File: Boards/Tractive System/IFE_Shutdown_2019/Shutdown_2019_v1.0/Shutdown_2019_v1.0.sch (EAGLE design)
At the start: 6 parts, among them J1 USB_, U1 FT232RLSSOP

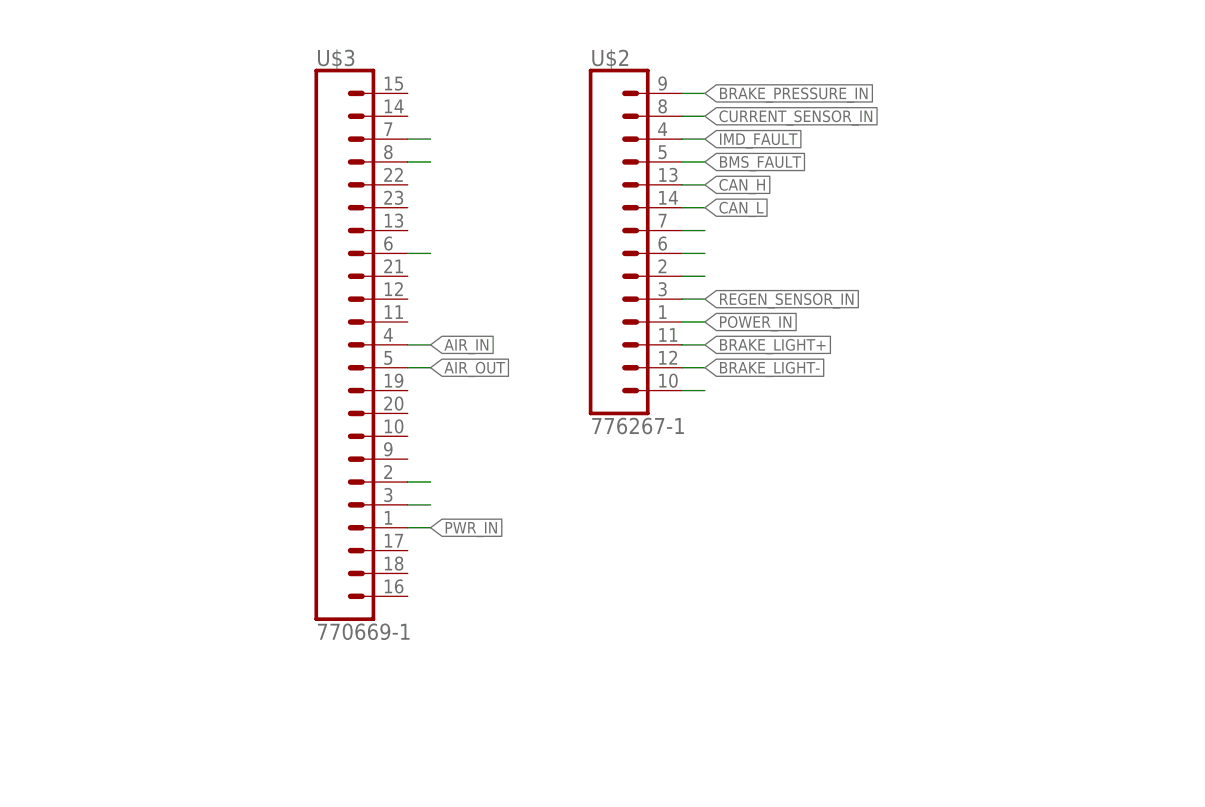
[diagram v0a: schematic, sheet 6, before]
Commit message: Adjusted precharge relay package, reduced area
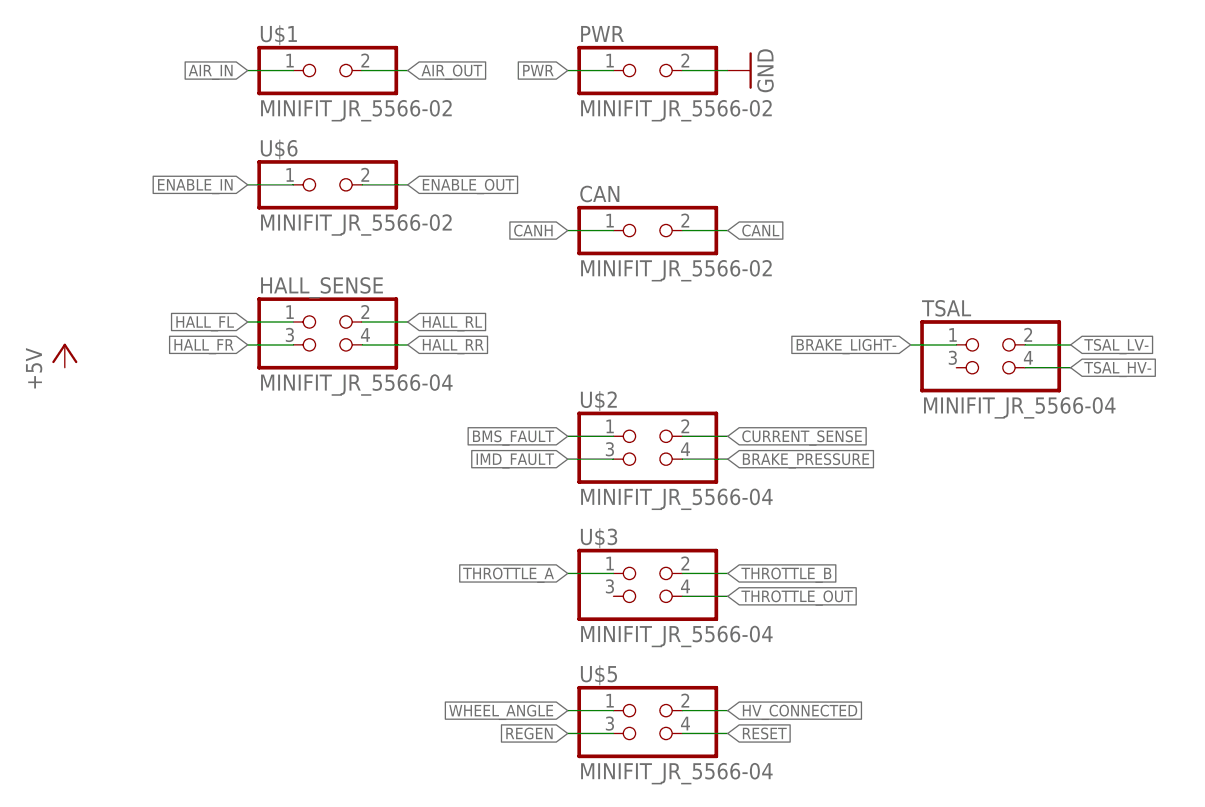
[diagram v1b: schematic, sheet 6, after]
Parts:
- removed J1: USB_, SparkFun-Connectors:USB_
- removed U1: FT232RLSSOP, SparkFun-DigitalIC:FT232RLSSOP
- added !BSPD_FAULT, !CONFLICT, BCO, BTH, TCO, TTH: TPTP09R, testpad:TPTP09R
- added BRAKE, THROTTLE: RTRIM3249W, Resistors:RTRIM3249W
- added C18: 10uF, Capacitors:C0805
- added C19: 0.01uF, Capacitors:C0805
- added C24: 0.1uF, Capacitors:C0805
- added CAN, PWR, U$6: MINIFIT_JR_5566-02, Display_Custom:MINIFIT_JR_5566-02
- added HALL_SENSE, TSAL, U$5: MINIFIT_JR_5566-04, Display_Custom:MINIFIT_JR_5566-04
- added IC1: LM555D, bspd2:LM555D
- added IC3: LM393D, IC's:LM393D
- added Q1, Q2: IRLML6346PBF, TRANS:IRLML6346PBF
- added R10: 1k, Resistors:R0805
- added R13: 50k, Resistors:R0805
- added R14, R33, R38, R39, R40, R8: 10k, Resistors:R0805
- added R9: 100k, Resistors:R0805
- added U$11: SN74LVC1G04DBVR, Display_Custom:SN74LVC1G04DBVR
- added U$7, U$8: IRLL024ZPBF, Display_Custom:IRLL024ZPBF
- added U$9: SN74LVC1G132DBVR, Display_Custom:SN74LVC1G132DBVR
- U$1: value ATTINY84ATTINY84-20MU -> MINIFIT_JR_5566-02; device SparkFun-DigitalIC:ATTINY84ATTINY84-20MU -> Display_Custom:MINIFIT_JR_5566-02
- U$2: value 776267-1 -> MINIFIT_JR_5566-04; device IFE_AMPSEAL_Conn:776267-1 -> Display_Custom:MINIFIT_JR_5566-04
- U$3: value 770669-1 -> MINIFIT_JR_5566-04; device IFE_AMPSEAL_Conn:770669-1 -> Display_Custom:MINIFIT_JR_5566-04
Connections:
- net POWER_IN renamed BRAKE_PRESSURE
- removed net BRAKE_LIGHT+: U$2.3
- removed net BRAKE_PRESSURE_IN: U$2.14
- removed net CAN_H: U$2.10
- removed net CAN_L: U$2.9
- removed net CURRENT_SENSOR_IN: U$2.13
- removed net N$1: U$2.8
- removed net N$2: U$2.7
- removed net N$4: U$2.1
- removed net N$8: U$3.22
- removed net N$9: U$3.17
- removed net PWR_IN: U$3.5
- removed net REGEN_SENSOR_IN: U$2.5
- new net !CONFLICT: !CONFLICT.TP, IC1.TR, R8.2, U$9.Y
- new net +12V: R10.1, R9.1
- new net +5V: BRAKE.A, C24.1, IC1.R, IC1.V+, IC3P.V+, R13.2, R14.2, R33.2, R38.2, R39.2, R40.1, R8.1, THROTTLE.A, U$11.V+, U$9.V+
- new net BRAKE_IN: IC3A.+IN, R33.1
- new net BSPD_FAULT: IC1.Q, U$11.A
- new net CANH: CAN.1
- new net CANL: CAN.2
- new net CURRENT_IN: IC3B.+IN, R14.1
- new net CURRENT_SENSE: U$2.2
- new net ENABLE_IN: U$6.1
- new net ENABLE_OUT: U$6.2
- new net FAULT_1_BSPD_IN: Q2.D, R10.2
- new net GND: BRAKE.E, C18.2, C19.2, C24.2, IC1.GND, IC3P.V-, PWR.2, Q1.S, Q2.S, THROTTLE.E, U$11.GND, U$9.GND
- new net HALL_FL: HALL_SENSE.1
- new net HALL_FR: HALL_SENSE.3
- new net HALL_RL: HALL_SENSE.2
- new net HALL_RR: HALL_SENSE.4
- new net HV_CONNECTED: U$5.2
- new net N$10: C18.1, IC1.DIS, IC1.THR, R13.1
- new net N$11: C19.1, IC1.CV
- new net N$15: Q1.D, Q2.G, R9.2
- new net N$16: IC3B.-IN, THROTTLE.S, TTH.TP
- new net PWR: PWR.1
- new net REGEN: U$5.3
- new net RESET: U$5.4
- new net THROTTLE_A: U$3.1
- new net THROTTLE_B: U$3.2
- new net THROTTLE_OUT: U$3.4
- new net TSAL_HV-: TSAL.4
- new net TSAL_LV-: TSAL.2
- new net WHEEL_ANGLE: U$5.1
- net AIR_IN: now also U$1.1; no longer U$3.13
- net AIR_OUT: now also U$1.2; no longer U$3.12
- net BMS_FAULT: now also U$2.1; no longer U$2.11
- net BRAKE_LIGHT-: now also TSAL.1; no longer U$2.2
- net IMD_FAULT: now also U$2.3; no longer U$2.12
- net N$3: now also IC3B.OUT, R39.1, TCO.TP, U$9.A; no longer U$2.6
- net N$5: now also BCO.TP, IC3A.OUT, R38.1, U$9.B; no longer U$3.21
- net N$6: now also BRAKE.S, BTH.TP, IC3A.-IN; no longer U$3.6
- net N$7: now also !BSPD_FAULT.TP, Q1.G, R40.2, U$11.Y; no longer U$3.7
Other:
- note added: "5V-12V Conversion"
- note added: "Brake Threshold Comparator"
- note added: "Conflict Timer"
- note added: "Current Threshold Comparator"

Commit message: More shutdown work
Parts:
- added BMS1, BSPD, IMD: 3.3v BLUE, led:LEDCHIPLED_0805
- added C1, C3, C4: 0.1uF, Capacitors:C0805
- added C14, C15, C16: 47uF, rcl:CPOL-USUD-6,3X5,8
- added D15, D2, D9: 1N914, Diodes:1N914
- added D3, D5, D6: SMAJ12A, Diodes:SMAJ12A
- added Q11, Q15, Q6: DMP3099L-7, TRANS:DMP3099L-7
- added Q16, Q3, Q5: DMN6140L-7, TRANS:DMN6140L-7
- added R1, R19, R24: 10k, Resistors:R0805
- added R11, R20, R23: 300, Resistors:R0805
- added R3, R5, R6: 100k, Resistors:R0805
- added R36: 1k, Resistors:R0805
- added U$10, U$12, U$13: PCN-112D3MHZ, Display_Custom:PCN-112D3MHZ
- U$4, U$7, U$8: value IRLL024ZPBF -> RT424012; device Display_Custom:IRLL024ZPBF -> Display_Custom:RT424012
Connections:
- new net BMS1_FAULT_INDICATOR: C15.+, D9.C, R20.1, U$7.2_CENTER, U$7.COIL+
- new net BSPD_FAULT_INDICATOR: C16.+, D2.C, R11.1, U$4.2_CENTER, U$4.COIL+
- new net FAULT_2_BMS: Q3.G, R1.2
- new net FAULT_3_BMS2_IN: C3.1, D5.C, R5.2
- new net FAULT_4_IMD_IN: C4.1, D6.C, Q16.G, R24.2, R6.2
- new net FAULT_RESET: Q11.G, Q15.G, Q6.G, R36.2
- new net IMD_FAULT_INDICATOR: C14.+, D15.C, R23.1, U$8.2_CENTER, U$8.COIL+
- new net N$1: C15.-, D9.A, Q3.D, U$7.COIL-
- new net N$27: U$4.1_ACTIVE, U$7.1_CENTER
- new net N$28: Q6.D, U$4.2_REST
- new net N$31: U$7.1_ACTIVE, U$8.1_CENTER
- new net N$32: C16.-, D2.A, Q5.D, U$4.COIL-
- new net N$34: BMS1.A, R20.2
- new net N$35: Q11.D, U$7.2_REST
- new net N$42: IMD.A, R23.2
- new net N$43: Q15.D, U$8.2_REST
- new net N$44: C14.-, D15.A, Q16.D, U$8.COIL-
- new net N$8: BSPD.A, R11.2
- net +12V: now also Q11.S, Q15.S, Q6.S, R36.1, U$4.2_ACTIVE, U$7.2_ACTIVE, U$8.2_ACTIVE
- net AIR_IN: now also U$4.1_CENTER
- net AIR_OUT: now also U$8.1_ACTIVE
- net FAULT_1_BSPD_IN: now also C1.1, D3.C, Q5.G, R19.2, R3.2
- net GND: now also BMS1.C, BSPD.C, C1.2, C3.2, C4.2, D3.A, D5.A, D6.A, IMD.C, Q16.S, Q3.S, Q5.S, R1.1, R19.1, R24.1, R3.1, R5.1, R6.1
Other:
- note added: "FAULT_RESET Pull Up"
- note added: "Fault Circuitry Faults are Active Low Pull FAULT_RESET Low to Reset"
- note added: "Fault Input Filter"

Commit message: Adding circuitry to shutdown, relay drivers
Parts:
- removed U$12: PCN-112D3MHZ, Display_Custom:PCN-112D3MHZ
- added H1, H2, H3, H4: MOUNT-PAD-ROUND3.0, holes:MOUNT-PAD-ROUND3.0
- added Q4, Q7, Q8: DMN6140L-7, TRANS:DMN6140L-7
- added R2, R4, R7: 10k, Resistors:R0805
- added R_RTD: PCN-112D3MHZ, Display_Custom:PCN-112D3MHZ
- added U1, U2: STM32F103CBT6, ST Microelctronics_By_element14_Batch_1:STM32F103CBT6
- renumbered BMS1 to BMS, U$10 to R_APPS, U$13 to R_BTSF, U$4 to R_BSPD, U$7 to R_BMS, U$8 to R_IMD
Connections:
- new net APPS_EN: Q4.G, R2.2
- new net BTSF_EN: Q7.G, R4.2
- new net N$12: R_BTSF.3, R_RTD.4
- new net N$13: R_APPS.3, R_BTSF.4
- new net N$2: Q4.D, R_APPS.2
- new net N$4: Q7.D, R_BTSF.2
- new net N$9: Q8.D, R_RTD.2
- new net PRECHARGE_COMPLETE: U$3.3
- new net RTDS-: TSAL.3
- new net RTD_EN: Q8.G, R7.2
- net ENABLE_IN: now also R_APPS.4
- net ENABLE_OUT: now also R_RTD.3
- net GND: now also H1.MOUNT, H2.MOUNT, H3.MOUNT, H4.MOUNT, Q4.S, Q7.S, Q8.S, R2.1, R4.1, R7.1

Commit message: Safety board cleanup
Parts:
- removed !BSPD_FAULT, !CONFLICT, BCO, BTH, TCO, TTH: TPTP09R, testpad:TPTP09R
- removed BMS, BSPD, IMD: 3.3v BLUE, led:LEDCHIPLED_0805
- removed BRAKE, THROTTLE: RTRIM3249W, Resistors:RTRIM3249W
- removed C18: 10uF, Capacitors:C0805
- removed C19: 0.01uF, Capacitors:C0805
- removed C24: 0.1uF, Capacitors:C0805
- removed IC1: LM555D, bspd2:LM555D
- removed IC3: LM393D, IC's:LM393D
- removed Q1, Q2: IRLML6346PBF, TRANS:IRLML6346PBF
- removed R13: 50k, Resistors:R0805
- removed R14, R19, R24, R33, R38, R39, R40: 10k, Resistors:R0805
- removed R20, R23: 300, Resistors:R0805
- removed R3, R6, R9: 100k, Resistors:R0805
- removed R36: 1k, Resistors:R0805
- removed U$11: SN74LVC1G04DBVR, Display_Custom:SN74LVC1G04DBVR
- removed U$9: SN74LVC1G132DBVR, Display_Custom:SN74LVC1G132DBVR
- removed U2: STM32F103CBT6, ST Microelctronics_By_element14_Batch_1:STM32F103CBT6
- added BRAKE1, THROTTLE1: RTRIM3249W, Resistors:RTRIM3249W
- added BTH1, TTH1: TPTP09R, testpad:TPTP09R
- added C5, C6, C7: 0.1u, resistor:C-USC0603
- added D1, D4, D7: BLUE, SparkFun-LED:LED-BLUE0603
- added Q12, Q13, Q14, Q17: IRLML6346PBF, TRANS:IRLML6346PBF
- added R15, R21, R22: 900, resistor:R-US_R0603
- added R16, R17, R18, R25: 10k, resistor:R-US_R0603
- C1: value 0.1uF -> 0.1u; device Capacitors:C0805 -> resistor:C-USC0603
- C3, C4: value 0.1uF -> 3u; device Capacitors:C0805 -> resistor:C-USC0603
- D3, D5, D6: value SMAJ12A -> 1N914; device Diodes:SMAJ12A -> Diodes:1N914
- R1: value 10k -> 100k; device Resistors:R0805 -> resistor:R-US_R0603
- R10: value 1k -> 10k; device Resistors:R0805 -> resistor:R-US_R0603
- R11: value 300 -> 100k; device Resistors:R0805 -> resistor:R-US_R0603
- R5: value 100k -> 10k; device Resistors:R0805 -> resistor:R-US_R0603
- R8: device Resistors:R0805 -> resistor:R-US_R0603
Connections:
- removed net !CONFLICT: !CONFLICT.TP, IC1.TR, R8.2, U$9.Y
- removed net BSPD_FAULT: IC1.Q, U$11.A
- removed net FAULT_1_BSPD_IN: C1.1, D3.C, Q2.D, Q5.G, R10.2, R19.2, R3.2
- removed net FAULT_2_BMS: Q3.G, R1.2
- removed net FAULT_3_BMS2_IN: C3.1, D5.C, R5.2
- removed net FAULT_4_IMD_IN: C4.1, D6.C, Q16.G, R24.2, R6.2
- removed net N$15: Q1.D, Q2.G, R9.2
- removed net N$16: IC3B.-IN, THROTTLE.S, TTH.TP
- removed net N$3: IC3B.OUT, R39.1, TCO.TP, U$9.A
- removed net N$5: BCO.TP, IC3A.OUT, R38.1, U$9.B
- removed net N$6: BRAKE.S, BTH.TP, IC3A.-IN
- new net BRAKE_TH: BRAKE1.S, BTH1.TP
- new net BSPD_FAULT_INDICATOR1: D3.C
- new net BSPD_FAULT_INDICATOR2: D5.C
- new net BSPD_FAULT_INDICATOR3: D6.C
- new net FAULT_BMS: C6.1, Q3.G, R17.2
- new net FAULT_BSPD: C7.1, Q12.D, Q14.D, Q17.D, Q5.G, R16.2, R5.1
- new net FAULT_IMD: C5.1, Q16.G, R18.2
- new net THROTTLE_TH: THROTTLE1.S, TTH1.TP
- net +12V: now also R25.2, R5.2; no longer R10.1, R36.1, R9.1
- net +5V: now also BRAKE1.A, C1.1, R1.2, R10.2, R11.2, R8.2, THROTTLE1.A; no longer BRAKE.A, C24.1, IC1.R, IC1.V+, IC3P.V+, R13.2, R14.2, R33.2, R38.2, R39.2, R40.1, R8.1, THROTTLE.A, U$11.V+, U$9.V+
- net BMS1_FAULT_INDICATOR: now also R22.1; no longer R20.1
- net BRAKE_IN: now also R10.1; no longer IC3A.+IN, R33.1
- net BSPD_FAULT_INDICATOR: now also R15.1; no longer R11.1
- net CURRENT_IN: now also R8.1; no longer IC3B.+IN, R14.1
- net FAULT_RESET: now also R25.1; no longer R36.2
- net GND: now also BRAKE1.E, C14.-, C15.-, C16.-, C5.2, C6.2, C7.2, D1.C, D4.C, D7.C, Q13.S, Q14.S, Q17.S, R16.1, R17.1, R18.1, THROTTLE1.E; no longer BMS.C, BRAKE.E, BSPD.C, C18.2, C19.2, C24.2, D3.A, D5.A, D6.A, IC1.GND, IC3P.V-, IMD.C, Q1.S, Q2.S, R1.1, R19.1, R24.1, R3.1, R5.1, R6.1, THROTTLE.E, U$11.GND, U$9.GND
- net IMD_FAULT_INDICATOR: now also R21.1; no longer R23.1
- net N$1: no longer C15.-
- net N$10: now also D5.A, Q7.D, R_BTSF.2; no longer C18.1, IC1.DIS, IC1.THR, R13.1
- net N$11: now also D6.A, Q8.D, R_RTD.2; no longer C19.1, IC1.CV
- net N$2: now also C3.1, R11.1; no longer Q4.D, R_APPS.2
- net N$32: no longer C16.-
- net N$34: now also D4.A, R22.2; no longer BMS.A, R20.2
- net N$4: now also C4.1, R1.1; no longer Q7.D, R_BTSF.2
- net N$42: now also D1.A, R21.2; no longer IMD.A, R23.2
- net N$44: no longer C14.-
- net N$7: now also D3.A, Q4.D, R_APPS.2; no longer !BSPD_FAULT.TP, Q1.G, R40.2, U$11.Y
- net N$8: now also D7.A, R15.2; no longer BSPD.A, R11.2
- net N$9: now also Q12.S, Q13.D; no longer Q8.D, R_RTD.2
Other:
- note removed: "5V-12V Conversion"
- note removed: "Brake Threshold Comparator"
- note removed: "Conflict Timer"
- note removed: "Current Threshold Comparator"
- note removed: "FAULT_RESET Pull Up"
- note removed: "Fault Circuitry Faults are Active Low Pull FAULT_RESET Low to Reset"
- note removed: "Fault Input Filter"

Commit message: Working on Power Supply and Light Drivers for Safety Board
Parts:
- added U$4, U$7, U$8: DNBT8105, DIODES_INC:DNBT8105
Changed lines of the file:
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@@
 <part name="FRAME8" library="frames" library_urn="urn:adsk.eagle:library:229" deviceset="FRAME_B_L" device=""/>
 <part name="FRAME9" library="frames" library_urn="urn:adsk.eagle:library:229" deviceset="FRAME_B_L" device=""/>
+<part name="U$4" library="DIODES_INC" deviceset="DNBT8105" device=""/>
+<part name="U$7" library="DIODES_INC" deviceset="DNBT8105" device=""/>
+<part name="U$8" library="DIODES_INC" deviceset="DNBT8105" device=""/>
 </parts>
 <sheets>
@@
 <instance part="FRAME4" gate="G$1" x="-208.28" y="-129.54"/>
 <instance part="FRAME4" gate="G$2" x="116.84" y="-129.54"/>
+<instance part="U$4" gate="G$1" x="35.56" y="20.32"/>
 </instances>
 <busses>
@@
 <instance part="FRAME5" gate="G$1" x="-205.74" y="-132.08"/>
 <instance part="FRAME5" gate="G$2" x="119.38" y="-132.08"/>
+<instance part="U$7" gate="G$1" x="48.26" y="33.02"/>
+<instance part="U$8" gate="G$1" x="48.26" y="-10.16"/>
 </instances>
 <busses>

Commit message: Finishing power distribution on safety board
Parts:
- removed C15, C16: 47uF, rcl:CPOL-USUD-6,3X5,8
- added C10: 220u, rcl:CPOL-USE2.5-7
- added C11: 2.2u, rcl:C-USC0805
- added C12, C13: 4.7u, rcl:C-USC0805
- added C2, C8, C9: 47u, rcl:CPOL-USE2.5-7
- added CURRENT_SENSOR_SUPPLY: MINIFIT_JR_5566-02, Display_Custom:MINIFIT_JR_5566-02
- added FUSE: MINI297-3568, Fuse:MINI297-3568
- added JP1: (no value), Headers_IFE:PINHD-1X4
- added L1, L2: 10u, SparkFun-Passives:INDUCTOR
- added Q1, Q2, Q9: DMN6140L-7, TRANS:DMN6140L-7
- added R12, R13, R14: 10k, resistor:R-US_R0603
- added R3, R6: 3.6k, rcl:R-US_R0603
- added R9: (no value), rcl:R-US_R0603
- added U$10: SPX1117M3-L-5-0, MAXLINEAR:SPX1117M3-L-5-0
- added U$9: SPX1117M3-L-3-3, MAXLINEAR:SPX1117M3-L-3-3
- C14: value 47uF -> 2.2u; device rcl:CPOL-USUD-6,3X5,8 -> rcl:C-USC0805
- R2, R4, R7: device Resistors:R0805 -> rcl:R-US_R0603
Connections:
- removed net BMS1_FAULT_INDICATOR: C15.+, D9.C, R22.1, R_BMS.2_CENTER, R_BMS.COIL+
- removed net BSPD_FAULT_INDICATOR: C16.+, D2.C, R15.1, R_BSPD.2_CENTER, R_BSPD.COIL+
- removed net BSPD_FAULT_INDICATOR1: D3.C
- removed net BSPD_FAULT_INDICATOR2: D5.C
- removed net BSPD_FAULT_INDICATOR3: D6.C
- removed net IMD_FAULT_INDICATOR: C14.+, D15.C, R21.1, R_IMD.2_CENTER, R_IMD.COIL+
- new net +3V3: C11.1, R12.2, R13.2, R14.2, U$9.VOUT
- new net BRAKE_LIGHT_EN: R9.1
- new net FAULT_BMS_STAT: C8.+, D9.C, R22.1, R_BMS.2_CENTER, R_BMS.COIL+
- new net FAULT_BMS_STATUS: Q2.G
- new net FAULT_BMS_STATUS_3_3: Q2.D, R13.1
- new net FAULT_BSPD_STAT: C2.+, D2.C, R15.1, R_BSPD.2_CENTER, R_BSPD.COIL+
- new net FAULT_BSPD_STATUS: Q1.G
- new net FAULT_BSPD_STATUS_3_3: Q1.D, R12.1
- new net FAULT_IMD_STAT: C9.+, D15.C, R21.1, R_IMD.2_CENTER, R_IMD.COIL+
- new net FAULT_IMD_STATUS: Q9.G
- new net FAULT_IMD_STATUS_3_3: Q9.D, R14.1
- new net N$15: R3.2, U$8.B
- new net N$16: R6.2, U$7.B
- new net N$3: R9.2, U$4.B
- new net N$5: C10.+, L1.1, L2.2
- new net N$6: FUSE.2, L2.1
- new net TSAL_HV_EN: R3.1
- new net TSAL_LV_EN: R6.1
- net +12V: now also C12.1, C13.1, D3.C, D5.C, D6.C, L1.2, R_APPS.1, R_BTSF.1, R_RTD.1, U$10.VIN, U$9.VIN
- net +5V: now also C14.1, CURRENT_SENSOR_SUPPLY.1, U$10.VOUT
- net BRAKE_LIGHT-: now also U$4.C
- net GND: now also C10.-, C11.2, C12.2, C13.2, C14.2, C2.-, C8.-, C9.-, CURRENT_SENSOR_SUPPLY.2, Q1.S, Q2.S, Q9.S, U$10.GND, U$4.E, U$7.E, U$8.E, U$9.GND; no longer C14.-, C15.-, C16.-
- net PWR: now also FUSE.1
- net TSAL_HV-: now also U$8.C
- net TSAL_LV-: now also U$7.C

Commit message: added CAN circuit and DEBUG headder
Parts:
- removed L1, L2: 10u, SparkFun-Passives:INDUCTOR
- added C15, C19: 1u, rcl:C-USC0805
- added C17, C18: 560p, rcl:C-USC0603
- added D10: RED, SparkFun-LED:LED-RED0603
- added D11, D12: GREEN, SparkFun-LED:LED-GREEN0603
- added D8: PESD1, diode:PESD1CAN
- added L4: 10u, microbuilder:INDUCTORNR5040
- added R19, R20: 100, rcl:R-US_R0603
- added R23: 4.7k, rcl:R-US_R0603
- added R24: 120, rcl:R-US_R0603
- added R26: 10k, rcl:R-US_R0603
- added U$11: MCP2551, Microchip_By_element14_Batch_1:MCP2551-I/SN
- JP1: device Headers_IFE:PINHD-1X4 -> Headers_IFE:PINHD-1X5
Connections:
- removed net N$5: C10.+, L1.1, L2.2
- new net !RST: JP1.2, R26.2, U1.NRST
- new net N$14: C17.1, R19.1
- new net N$17: C18.1, R20.1
- new net N$18: R23.1, U$11.RS
- new net RXCAN: U$11.RXD
- new net SWDCLK: JP1.4
- new net SWDIO: JP1.3
- new net TXCAN: U$11.TXD
- new net VDDA: U1.VDDA
- net +12V: now also C10.+, L4.2; no longer L1.2
- net +3V3: now also C15.1, C19.1, JP1.1, R26.1, U1.VDD_1, U1.VDD_2, U1.VDD_3
- net +5V: now also U$11.VDD
- net CANH: now also D8.1, R20.2, R24.2, U$11.CANH
- net CANL: now also D8.2, R19.2, R24.1, U$11.CANL
- net GND: now also C15.2, C17.2, C18.2, C19.2, D8.3, JP1.5, R23.2, U$11.VSS, U1.BOOT0, U1.PB2, U1.VSSA, U1.VSS_1, U1.VSS_2, U1.VSS_3
- net N$6: now also L4.1; no longer L2.1
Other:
- moved on the sheet: C2, C5, C6, C7, C8, C9, D1, D15, D2, D4, D7, D9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
